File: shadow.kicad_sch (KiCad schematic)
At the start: 18 parts, among them SW1 SW_Push, SW2 SW_Push

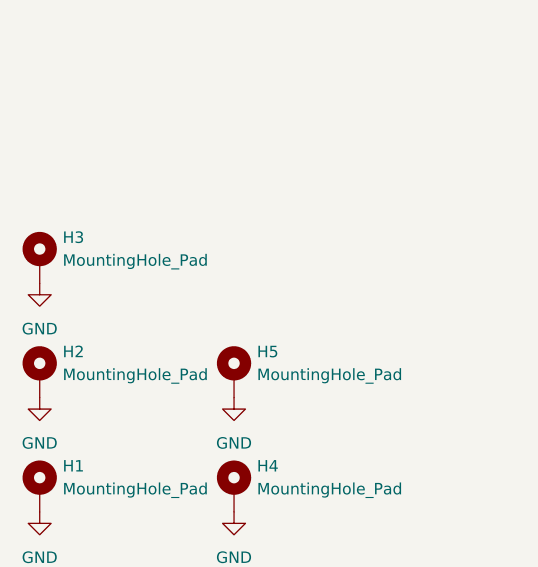
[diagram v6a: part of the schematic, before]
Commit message: move all backside components to front and make it work for jlc basic components
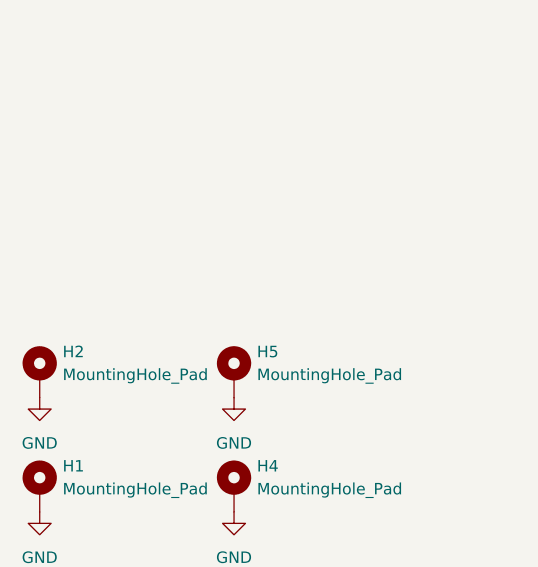
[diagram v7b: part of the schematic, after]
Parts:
- removed H3: MountingHole_Pad, MountingHole:MountingHole_4.3mm_M4_DIN965_Pad, symbol Mechanical:MountingHole_Pad
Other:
- sheet I2C_PINOUT renamed I2C
- sheet I2C_PINOUT1 renamed I2C1
- sheet I2C_PINOUT10 renamed I2C10
- sheet I2C_PINOUT11 renamed I2C11
- sheet I2C_PINOUT12 renamed I2C12
- sheet I2C_PINOUT2 renamed I2C2
- sheet I2C_PINOUT3 renamed I2C3
- sheet I2C_PINOUT4 renamed I2C4
- sheet I2C_PINOUT5 renamed I2C5
- sheet I2C_PINOUT6 renamed I2C6
- sheet I2C_PINOUT7 renamed I2C7
- sheet I2C_PINOUT8 renamed I2C8
- sheet I2C_PINOUT9 renamed I2C9
- sheet I2C: file I2C_PINOUT.kicad_sch -> I2C.kicad_sch
- sheet I2C1: file I2C_PINOUT.kicad_sch -> I2C.kicad_sch
- sheet I2C10: file I2C_PINOUT.kicad_sch -> I2C.kicad_sch
- sheet I2C11: file I2C_PINOUT.kicad_sch -> I2C.kicad_sch
- sheet I2C12: file I2C_PINOUT.kicad_sch -> I2C.kicad_sch
- sheet I2C2: file I2C_PINOUT.kicad_sch -> I2C.kicad_sch
- sheet I2C3: file I2C_PINOUT.kicad_sch -> I2C.kicad_sch
- sheet I2C4: file I2C_PINOUT.kicad_sch -> I2C.kicad_sch
- sheet I2C5: file I2C_PINOUT.kicad_sch -> I2C.kicad_sch
- sheet I2C6: file I2C_PINOUT.kicad_sch -> I2C.kicad_sch
- sheet I2C7: file I2C_PINOUT.kicad_sch -> I2C.kicad_sch
- sheet I2C8: file I2C_PINOUT.kicad_sch -> I2C.kicad_sch
- sheet I2C9: file I2C_PINOUT.kicad_sch -> I2C.kicad_sch
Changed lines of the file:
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@@
 	)
 	(symbol
-		(lib_id "power:GND")
-		(at 21.59 162.56 0)
-		(unit 1)
-		(exclude_from_sim no)
-		(in_bom yes)
-		(on_board yes)
-		(dnp no)
-		(fields_autoplaced yes)
-		(property "Reference" "#PWR021"
-			(at 21.59 168.91 0)
-			(effects
-				(font
-					(size 1.27 1.27)
-				)
-				(hide yes)
-			)
-		)
-		(property "Value" "GND"
-			(at 21.59 167.64 0)
-			(effects
-				(font
-					(size 1.27 1.27)
-				)
-			)
-		)
-		(property "Footprint" ""
-			(at 21.59 162.56 0)
-			(effects
-				(font
-					(size 1.27 1.27)
-				)
-				(hide yes)
-			)
-		)
-		(property "Datasheet" ""
-			(at 21.59 162.56 0)
-			(effects
-				(font
-					(size 1.27 1.27)
-				)
-				(hide yes)
-			)
-		)
-		(property "Description" "Power symbol creates a global label with name \"GND\" , ground"
-			(at 21.59 162.56 0)
-			(effects
-				(font
-					(size 1.27 1.27)
-				)
-				(hide yes)
-			)
-		)
-		(pin "1"
-		)
-		(instances
-			(project "shadow"
-				(path "/3c2fce68-ba60-4bda-a294-ddd60ff77106"
-					(reference "#PWR021")
-					(unit 1)
-				)
-			)
-		)
-	)
-	(symbol
 		(lib_id "Connector_Generic:Conn_01x15")
 		(at 138.43 109.22 0)
@@
 	)
 	(symbol
-		(lib_id "Mechanical:MountingHole_Pad")
-		(at 21.59 160.02 0)
-		(unit 1)
-		(exclude_from_sim yes)
-		(in_bom no)
-		(on_board yes)
-		(dnp no)
-		(fields_autoplaced yes)
-		(property "Reference" "H3"
-			(at 24.13 157.4799 0)
-			(effects
-				(font
-					(size 1.27 1.27)
-				)
-				(justify left)
-			)
-		)
-		(property "Value" "MountingHole_Pad"
-			(at 24.13 160.0199 0)
-			(effects
-				(font
-					(size 1.27 1.27)
-				)
-				(justify left)
-			)
-		)
-		(property "Footprint" "MountingHole:MountingHole_4.3mm_M4_DIN965_Pad"
-			(at 21.59 160.02 0)
-			(effects
-				(font
-					(size 1.27 1.27)
-				)
-				(hide yes)
-			)
-		)
-		(property "Datasheet" "~"
-			(at 21.59 160.02 0)
-			(effects
-				(font
-					(size 1.27 1.27)
-				)
-				(hide yes)
-			)
-		)
-		(property "Description" "Mounting Hole with connection"
-			(at 21.59 160.02 0)
-			(effects
-				(font
-					(size 1.27 1.27)
-				)
-				(hide yes)
-			)
-		)
-		(pin "1"
-		)
-		(instances
-			(project "shadow"
-				(path "/3c2fce68-ba60-4bda-a294-ddd60ff77106"
-					(reference "H3")
-					(unit 1)
-				)
-			)
-		)
-	)
-	(symbol
 		(lib_id "power:VCC")
 		(at 231.14 82.55 90)
@@
 			(color 0 0 0 0.0000)
 		)
-		(property "Sheetname" "I2C_PINOUT8"
+		(property "Sheetname" "I2C8"
 			(at 157.48 43.7384 0)
 			(effects
@@
 			)
 		)
-		(property "Sheetfile" "I2C_PINOUT.kicad_sch"
+		(property "Sheetfile" "I2C.kicad_sch"
 			(at 157.48 48.8446 0)
 			(effects
@@
 			(color 0 0 0 0.0000)
 		)
-		(property "Sheetname" "I2C_PINOUT12"
+		(property "Sheetname" "I2C12"
 			(at 157.48 58.9784 0)
 			(effects
@@
 			)
 		)
-		(property "Sheetfile" "I2C_PINOUT.kicad_sch"
+		(property "Sheetfile" "I2C.kicad_sch"
 			(at 157.48 64.0846 0)
 			(effects
@@
 			(color 0 0 0 0.0000)
 		)
-		(property "Sheetname" "I2C_PINOUT10"
+		(property "Sheetname" "I2C10"
 			(at 157.48 51.3584 0)
 			(effects
@@
 			)
 		)
-		(property "Sheetfile" "I2C_PINOUT.kicad_sch"
+		(property "Sheetfile" "I2C.kicad_sch"
 			(at 157.48 56.4646 0)
 			(effects
@@
 			(color 0 0 0 0.0000)
 		)
-		(property "Sheetname" "I2C_PINOUT11"
+		(property "Sheetname" "I2C11"
 			(at 157.48 55.1684 0)
 			(effects
@@
 			)
 		)
-		(property "Sheetfile" "I2C_PINOUT.kicad_sch"
+		(property "Sheetfile" "I2C.kicad_sch"
 			(at 157.48 60.2746 0)
 			(effects
@@
 			(color 0 0 0 0.0000)
 		)
-		(property "Sheetname" "I2C_PINOUT1"
+		(property "Sheetname" "I2C1"
 			(at 241.3 36.1184 0)
 			(effects
@@
 			)
 		)
-		(property "Sheetfile" "I2C_PINOUT.kicad_sch"
+		(property "Sheetfile" "I2C.kicad_sch"
 			(at 241.3 41.2246 0)
 			(effects
@@
 			(color 0 0 0 0.0000)
 		)
-		(property "Sheetname" "I2C_PINOUT6"
+		(property "Sheetname" "I2C6"
 			(at 241.3 55.1684 0)
 			(effects
@@
 			)
 		)
-		(property "Sheetfile" "I2C_PINOUT.kicad_sch"
+		(property "Sheetfile" "I2C.kicad_sch"
 			(at 241.3 60.2746 0)
 			(effects
@@
 			(color 0 0 0 0.0000)
 		)
-		(property "Sheetname" "I2C_PINOUT"
+		(property "Sheetname" "I2C"
 			(at 241.3 32.3084 0)
 			(effects
@@
 			)
 		)
-		(property "Sheetfile" "I2C_PINOUT.kicad_sch"
+		(property "Sheetfile" "I2C.kicad_sch"
 			(at 241.3 37.4146 0)
 			(effects
@@
 			(color 0 0 0 0.0000)
 		)
-		(property "Sheetname" "I2C_PINOUT9"
+		(property "Sheetname" "I2C9"
 			(at 157.48 47.5484 0)
 			(effects
@@
 			)
 		)
-		(property "Sheetfile" "I2C_PINOUT.kicad_sch"
+		(property "Sheetfile" "I2C.kicad_sch"
 			(at 157.48 52.6546 0)
 			(effects
@@
 			(color 0 0 0 0.0000)
 		)
-		(property "Sheetname" "I2C_PINOUT5"
+		(property "Sheetname" "I2C5"
 			(at 241.3 51.3584 0)
 			(effects
@@
 			)
 		)
-		(property "Sheetfile" "I2C_PINOUT.kicad_sch"
+		(property "Sheetfile" "I2C.kicad_sch"
 			(at 241.3 56.4646 0)
 			(effects
@@
 			(color 0 0 0 0.0000)
 		)
-		(property "Sheetname" "I2C_PINOUT4"
+		(property "Sheetname" "I2C4"
 			(at 241.3 47.5484 0)
 			(effects
@@
 			)
 		)
-		(property "Sheetfile" "I2C_PINOUT.kicad_sch"
+		(property "Sheetfile" "I2C.kicad_sch"
 			(at 241.3 52.6546 0)
 			(effects
@@
 			(color 0 0 0 0.0000)
 		)
-		(property "Sheetname" "I2C_PINOUT3"
+		(property "Sheetname" "I2C3"
 			(at 241.3 43.7384 0)
 			(effects
@@
 			)
 		)
-		(property "Sheetfile" "I2C_PINOUT.kicad_sch"
+		(property "Sheetfile" "I2C.kicad_sch"
 			(at 241.3 48.8446 0)
 			(effects
@@
 			(color 0 0 0 0.0000)
 		)
-		(property "Sheetname" "I2C_PINOUT7"
+		(property "Sheetname" "I2C7"
 			(at 241.3 58.9784 0)
 			(effects
@@
 			)
 		)
-		(property "Sheetfile" "I2C_PINOUT.kicad_sch"
+		(property "Sheetfile" "I2C.kicad_sch"
 			(at 241.3 64.0846 0)
 			(effects
@@
 			(color 0 0 0 0.0000)
 		)
-		(property "Sheetname" "I2C_PINOUT2"
+		(property "Sheetname" "I2C2"
 			(at 241.3 39.9284 0)
 			(effects
@@
 			)
 		)
-		(property "Sheetfile" "I2C_PINOUT.kicad_sch"
+		(property "Sheetfile" "I2C.kicad_sch"
 			(at 241.3 45.0346 0)
 			(effects
